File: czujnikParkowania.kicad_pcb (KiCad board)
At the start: 2 copper layers, 43 parts, among them J1 Screw_Terminal_01x03, Q1 BC817, Q2 IRF7404, Q3 BC817, Q4 BC817, Q5 BC817, U1 DC56-11SEKWA, U2 LM7805_TO220, U3 HC-SR04, U4 ATmega328-AU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

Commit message: missing connections on PCB
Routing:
- net Net-(R9-Pad1): track 9.51 -> 28.3 mm, vias 0 -> 2
- net Net-(R10-Pad1): track 11.4 -> 24.3 mm, vias 0 -> 1
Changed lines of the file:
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@@
     (thickness 1.6)
     (drawings 0)
-    (tracks 368)
+    (tracks 382)
     (zones 0)
     (modules 43)
@@
   (segment (start 49.53 42.164) (end 49.53 43.1315) (width 0.25) (layer F.Cu) (net 36))
   (segment (start 48.5648 41.1988) (end 49.53 42.164) (width 0.25) (layer F.Cu) (net 36))
+  (via (at 40.005 34.29) (size 0.8) (drill 0.4) (layers F.Cu B.Cu) (net 36))
+  (segment (start 42.926 38.989) (end 42.926 37.211) (width 0.25) (layer F.Cu) (net 36))
+  (segment (start 42.926 37.211) (end 40.005 34.29) (width 0.25) (layer F.Cu) (net 36))
+  (via (at 36.83 34.29) (size 0.8) (drill 0.4) (layers F.Cu B.Cu) (net 36))
+  (segment (start 40.005 34.29) (end 36.83 34.29) (width 0.25) (layer B.Cu) (net 36))
+  (segment (start 36.83 34.29) (end 33.02 34.29) (width 0.25) (layer F.Cu) (net 36))
+  (segment (start 30.226 37.084) (end 30.226 38.989) (width 0.25) (layer F.Cu) (net 36))
+  (segment (start 33.02 34.29) (end 30.226 37.084) (width 0.25) (layer F.Cu) (net 36))
   (segment (start 46.228 43.1315) (end 45.477498 43.1315) (width 0.25) (layer F.Cu) (net 37))
   (segment (start 37.846 38.989) (end 37.846 38.481) (width 0.25) (layer F.Cu) (net 37))
@@
   (segment (start 45.0065 41.91) (end 46.228 43.1315) (width 0.25) (layer F.Cu) (net 37))
   (segment (start 42.8244 41.91) (end 45.0065 41.91) (width 0.25) (layer F.Cu) (net 37))
+  (via (at 33.655 36.83) (size 0.8) (drill 0.4) (layers F.Cu B.Cu) (net 37))
+  (segment (start 27.686 38.989) (end 29.845 36.83) (width 0.25) (layer B.Cu) (net 37))
+  (segment (start 29.845 36.83) (end 33.655 36.83) (width 0.25) (layer B.Cu) (net 37))
+  (segment (start 37.846 37.211) (end 37.846 38.989) (width 0.25) (layer F.Cu) (net 37))
+  (segment (start 33.655 36.83) (end 37.465 36.83) (width 0.25) (layer F.Cu) (net 37))
+  (segment (start 37.465 36.83) (end 37.846 37.211) (width 0.25) (layer F.Cu) (net 37))
   (segment (start 35.306 40.7416) (end 35.306 38.989) (width 0.25) (layer F.Cu) (net 38))
   (segment (start 26.4574 41.3004) (end 34.7472 41.3004) (width 0.25) (layer F.Cu) (net 38))

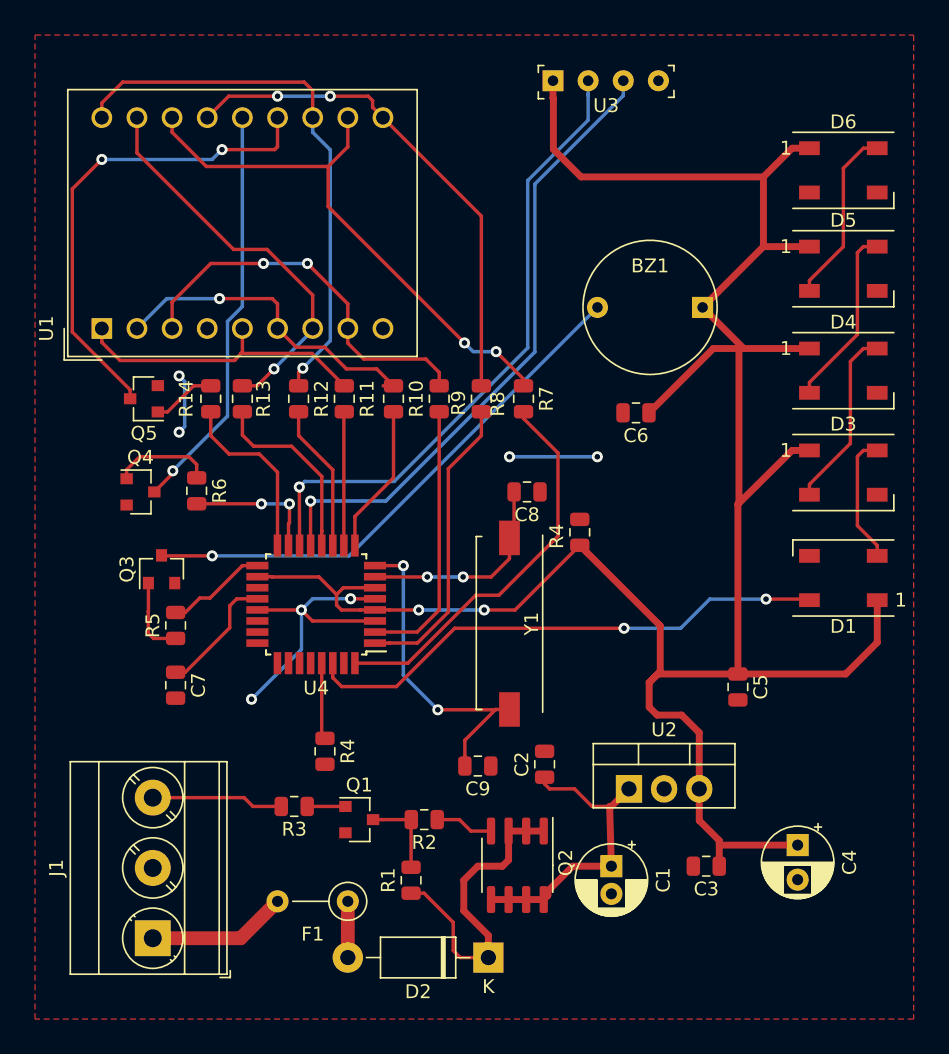
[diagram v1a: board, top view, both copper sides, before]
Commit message: added caps and button
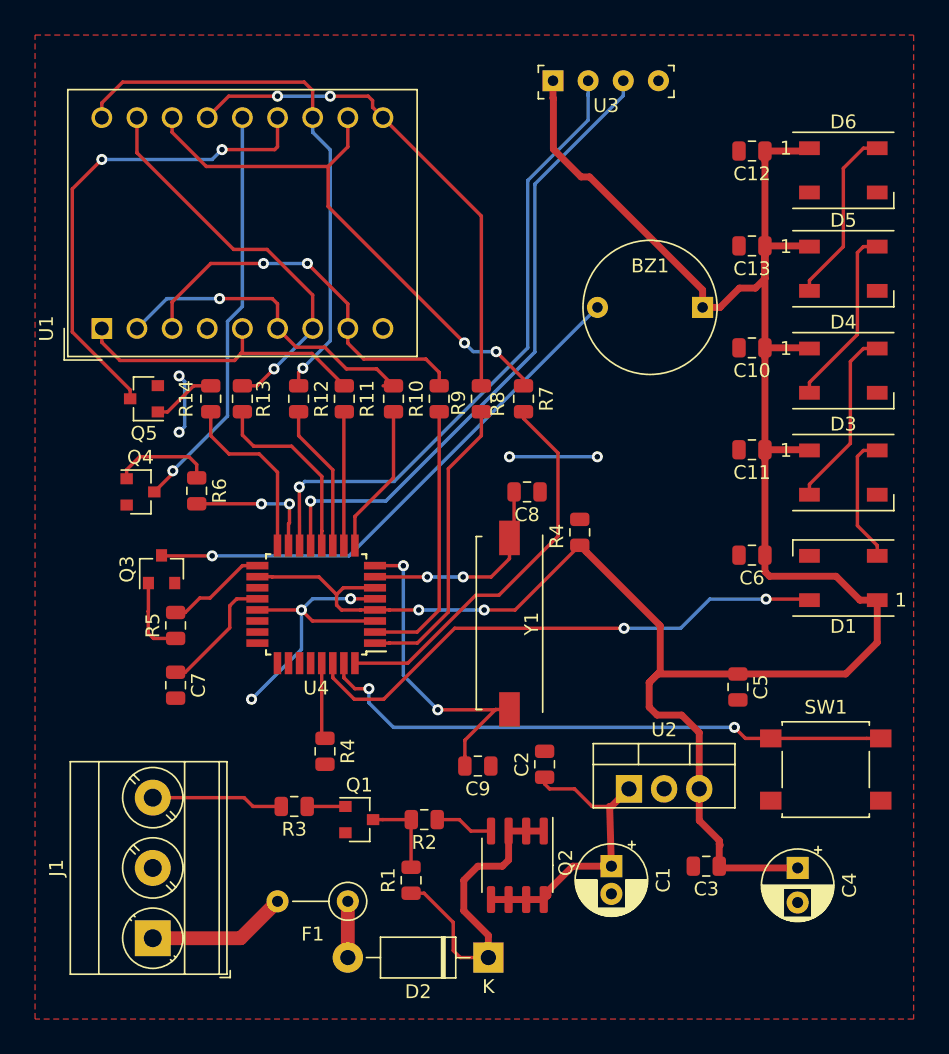
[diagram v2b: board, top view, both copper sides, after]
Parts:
- added C10: 100n, Capacitor_SMD:C_0805_2012Metric, F.Cu at (72.1, 40.4)
- added C11: 100n, Capacitor_SMD:C_0805_2012Metric, F.Cu at (72.1, 47.8)
- added C12: 100n, Capacitor_SMD:C_0805_2012Metric, F.Cu at (72.1, 26.2)
- added C13: 100n, Capacitor_SMD:C_0805_2012Metric, F.Cu at (72.1, 33.0)
- added SW1: SW_Push, Button_Switch_SMD:SW_SPST_B3S-1000, F.Cu at (77.5, 70.9)
- moved C6 13.3 mm to (72.1, 55.4)
- moved C4 1.65 mm to (75.4, 78.0)
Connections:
- U4 pad 31: /D1 -> /BTN
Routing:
- net /BTN: track 0.00 -> 42.3 mm, vias 0 -> 2
- net +5V: track 173.0 -> 166.7 mm
- net /RGB_DI: track 38.4 -> 39.2 mm

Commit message: added GND plane on back
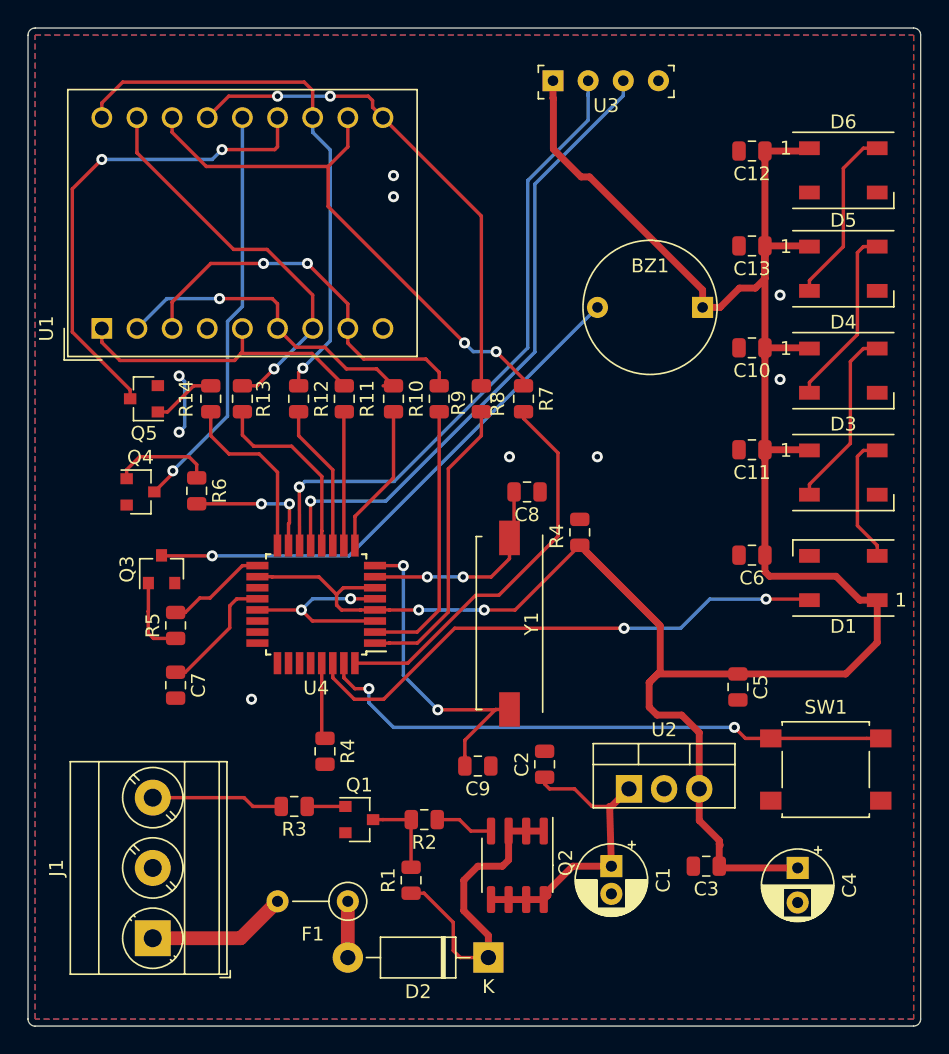
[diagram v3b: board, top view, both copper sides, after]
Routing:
- net GND: track 33.2 -> 18.9 mm, vias 7 -> 11
- net +5V: track 166.7 -> 174.1 mm
- added copper zone on B.Cu, net GND
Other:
- board outline added: 64.5 x 72.1 mm

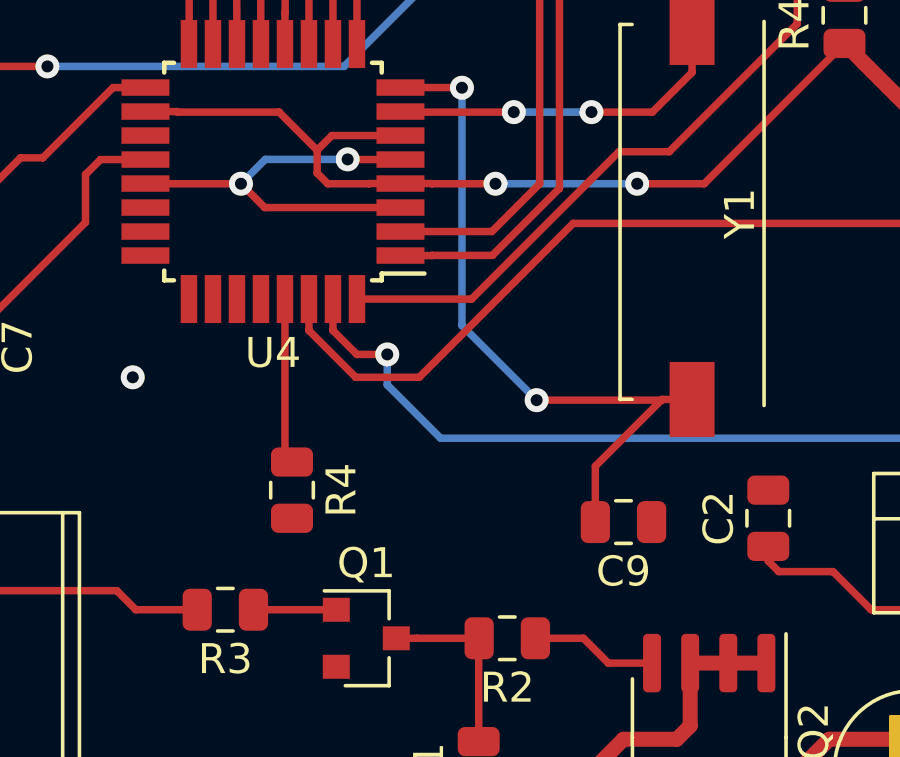
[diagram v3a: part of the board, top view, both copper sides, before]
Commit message: schematic reset pin bugfix
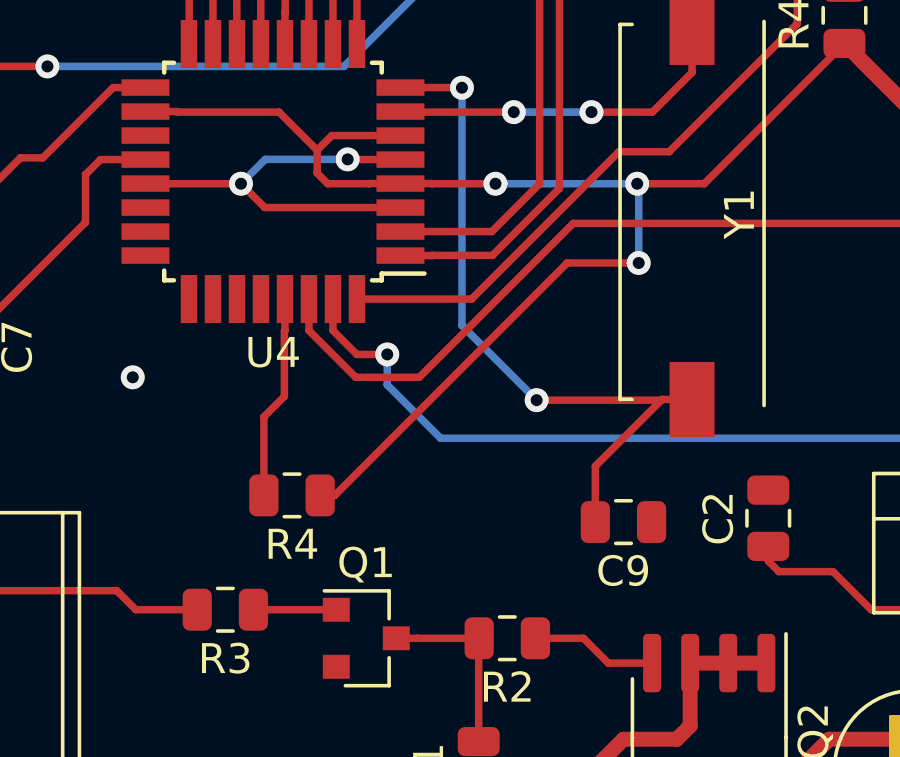
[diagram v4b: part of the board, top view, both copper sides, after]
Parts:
- moved R4 0.18 mm to (41.3, 69.7), turned to 180 degrees
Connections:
- R4 pad 1: Net-(R4-Pad1) -> +5V
- R4 pad 2: GND -> Net-(R4-Pad2)
- U4 pad 29: Net-(R4-Pad1) -> Net-(R4-Pad2)
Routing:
- net +5V: track 174.1 -> 190.6 mm, vias 2 -> 3
- net Net-(R4-Pad2): track 0.00 -> 6.84 mm
- net Net-(R4-Pad1): track 5.53 -> 0.00 mm
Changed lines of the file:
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@@
     (thickness 1.6)
     (drawings 8)
-    (tracks 408)
+    (tracks 417)
     (zones 0)
     (modules 48)
@@
   (net 46 "Net-(C8-Pad2)")
   (net 47 "Net-(C9-Pad2)")
-  (net 48 "Net-(R4-Pad1)")
-  (net 49 "Net-(U4-Pad19)")
-  (net 50 "Net-(U4-Pad22)")
-  (net 51 "Net-(U4-Pad23)")
-  (net 52 "Net-(U4-Pad24)")
-  (net 53 "Net-(U4-Pad25)")
-  (net 54 "Net-(U4-Pad26)")
-  (net 55 "Net-(U4-Pad27)")
-  (net 56 "Net-(U4-Pad28)")
-  (net 57 /BTN)
+  (net 48 "Net-(U4-Pad19)")
+  (net 49 "Net-(U4-Pad22)")
+  (net 50 "Net-(U4-Pad23)")
+  (net 51 "Net-(U4-Pad24)")
+  (net 52 "Net-(U4-Pad25)")
+  (net 53 "Net-(U4-Pad26)")
+  (net 54 "Net-(U4-Pad27)")
+  (net 55 "Net-(U4-Pad28)")
+  (net 56 /BTN)
+  (net 57 "Net-(R4-Pad2)")
   (net_class Default "To jest domyślna klasa połączeń."
     (clearance 0.2)
@@
     (add_net "Net-(R12-Pad1)")
     (add_net "Net-(R13-Pad1)")
-    (add_net "Net-(R4-Pad1)")
+    (add_net "Net-(R4-Pad2)")
     (add_net "Net-(R7-Pad1)")
     (add_net "Net-(R8-Pad1)")
@@
   )
   (module Resistor_SMD:R_0805_2012Metric (layer F.Cu)
-    (at 41.275 69.5475 270)
+    (at 41.275 69.723 180)
     (descr "Resistor SMD 0805 (2012 Metric), square (rectangular) end terminal, IPC_7351 nominal, (Body size source: https://docs.google.com/spreadsheets/d/1BsfQQcO9C6DZCsRaXUlFlo91Tg2WpOkGARC1WS5S8t0/edit?usp=sharing), generated with kicad-footprint-generator")
     (tags resistor)
     (attr smd)
-    (fp_text reference R4 (at 0 -1.65 90) (layer F.SilkS)
-      (effects (font (size 1 1) (thickness 0.15)))
-    )
-    (fp_text value 1k (at 0 1.65 90) (layer F.Fab)
+    (fp_text reference R4 (at 0 -1.65) (layer F.SilkS)
+      (effects (font (size 1 1) (thickness 0.15)))
+    )
+    (fp_text value 1k (at 0 1.65) (layer F.Fab)
       (effects (font (size 1 1) (thickness 0.15)))
     )
@@
     (fp_line (start 1.68 -0.95) (end 1.68 0.95) (layer F.CrtYd) (width 0.05))
     (fp_line (start 1.68 0.95) (end -1.68 0.95) (layer F.CrtYd) (width 0.05))
-    (fp_text user %R (at 0 0 90) (layer F.Fab)
+    (fp_text user %R (at 0 0) (layer F.Fab)
       (effects (font (size 0.5 0.5) (thickness 0.08)))
     )
-    (pad 1 smd roundrect (at -0.9375 0 270) (size 0.975 1.4) (layers F.Cu F.Paste F.Mask) (roundrect_rratio 0.25)
-      (net 48 "Net-(R4-Pad1)"))
-    (pad 2 smd roundrect (at 0.9375 0 270) (size 0.975 1.4) (layers F.Cu F.Paste F.Mask) (roundrect_rratio 0.25)
-      (net 4 GND))
+    (pad 1 smd roundrect (at -0.9375 0 180) (size 0.975 1.4) (layers F.Cu F.Paste F.Mask) (roundrect_rratio 0.25)
+      (net 2 +5V))
+    (pad 2 smd roundrect (at 0.9375 0 180) (size 0.975 1.4) (layers F.Cu F.Paste F.Mask) (roundrect_rratio 0.25)
+      (net 57 "Net-(R4-Pad2)"))
     (model ${KISYS3DMOD}/Resistor_SMD.3dshapes/R_0805_2012Metric.wrl
       (at (xyz 0 0 0))
@@
       (net 2 +5V))
     (pad 19 smd rect (at 4.25 1.2 180) (size 1.6 0.55) (layers F.Cu F.Paste F.Mask)
-      (net 49 "Net-(U4-Pad19)"))
+      (net 48 "Net-(U4-Pad19)"))
     (pad 20 smd rect (at 4.25 0.4 180) (size 1.6 0.55) (layers F.Cu F.Paste F.Mask)
       (net 45 "Net-(C7-Pad1)"))
@@
       (net 4 GND))
     (pad 22 smd rect (at 4.25 -1.2 180) (size 1.6 0.55) (layers F.Cu F.Paste F.Mask)
-      (net 50 "Net-(U4-Pad22)"))
+      (net 49 "Net-(U4-Pad22)"))
     (pad 23 smd rect (at 4.25 -2 180) (size 1.6 0.55) (layers F.Cu F.Paste F.Mask)
-      (net 51 "Net-(U4-Pad23)"))
+      (net 50 "Net-(U4-Pad23)"))
     (pad 24 smd rect (at 4.25 -2.8 180) (size 1.6 0.55) (layers F.Cu F.Paste F.Mask)
-      (net 52 "Net-(U4-Pad24)"))
+      (net 51 "Net-(U4-Pad24)"))
     (pad 25 smd rect (at 2.8 -4.25 270) (size 1.6 0.55) (layers F.Cu F.Paste F.Mask)
-      (net 53 "Net-(U4-Pad25)"))
+      (net 52 "Net-(U4-Pad25)"))
     (pad 26 smd rect (at 2 -4.25 270) (size 1.6 0.55) (layers F.Cu F.Paste F.Mask)
-      (net 54 "Net-(U4-Pad26)"))
+      (net 53 "Net-(U4-Pad26)"))
     (pad 27 smd rect (at 1.2 -4.25 270) (size 1.6 0.55) (layers F.Cu F.Paste F.Mask)
-      (net 55 "Net-(U4-Pad27)"))
+      (net 54 "Net-(U4-Pad27)"))
     (pad 28 smd rect (at 0.4 -4.25 270) (size 1.6 0.55) (layers F.Cu F.Paste F.Mask)
-      (net 56 "Net-(U4-Pad28)"))
+      (net 55 "Net-(U4-Pad28)"))
     (pad 29 smd rect (at -0.4 -4.25 270) (size 1.6 0.55) (layers F.Cu F.Paste F.Mask)
-      (net 48 "Net-(R4-Pad1)"))
+      (net 57 "Net-(R4-Pad2)"))
     (pad 30 smd rect (at -1.2 -4.25 270) (size 1.6 0.55) (layers F.Cu F.Paste F.Mask)
       (net 1 /RGB_DI))
     (pad 31 smd rect (at -2 -4.25 270) (size 1.6 0.55) (layers F.Cu F.Paste F.Mask)
-      (net 57 /BTN))
+      (net 56 /BTN))
     (pad 32 smd rect (at -2.8 -4.25 270) (size 1.6 0.55) (layers F.Cu F.Paste F.Mask)
       (net 5 /SEG_A))
@@
     (fp_line (start -3 3.3) (end -3 -3.3) (layer F.Fab) (width 0.1))
     (pad 1 smd rect (at -3.975 -2.25) (size 1.55 1.3) (layers F.Cu F.Paste F.Mask)
-      (net 57 /BTN))
+      (net 56 /BTN))
     (pad 1 smd rect (at 3.975 -2.25) (size 1.55 1.3) (layers F.Cu F.Paste F.Mask)
-      (net 57 /BTN))
+      (net 56 /BTN))
     (pad 2 smd rect (at -3.975 2.25) (size 1.55 1.3) (layers F.Cu F.Paste F.Mask)
       (net 4 GND))
@@
   (segment (start 65.44425 60.41275) (end 59.69 54.6585) (width 0.5) (layer F.Cu) (net 2) (status 20))
   (segment (start 65.44425 60.41275) (end 60.175527 55.144027) (width 0.5) (layer F.Cu) (net 2))
+  (segment (start 50.447 61.976) (end 52.832 61.976) (width 0.25) (layer F.Cu) (net 2))
+  (segment (start 42.2125 69.723) (end 42.7 69.723) (width 0.25) (layer F.Cu) (net 2))
+  (via (at 52.832 61.976) (size 0.8) (drill 0.4) (layers F.Cu B.Cu) (net 2))
+  (segment (start 42.7 69.723) (end 50.447 61.976) (width 0.25) (layer F.Cu) (net 2))
+  (segment (start 52.832 59.3852) (end 52.7812 59.3344) (width 0.25) (layer B.Cu) (net 2))
+  (segment (start 52.832 61.976) (end 52.832 59.3852) (width 0.25) (layer B.Cu) (net 2))
   (via (at 46.228 29.464) (size 0.8) (drill 0.4) (layers F.Cu B.Cu) (net 4))
   (via (at 46.228 27.94) (size 0.8) (drill 0.4) (layers F.Cu B.Cu) (net 4))
@@
   (segment (start 53.587 66.548) (end 53.61 66.525) (width 0.25) (layer F.Cu) (net 47))
   (segment (start 49.4284 66.548) (end 53.587 66.548) (width 0.25) (layer F.Cu) (net 47))
-  (segment (start 41.04 68.375) (end 41.275 68.61) (width 0.25) (layer F.Cu) (net 48) (status 30))
-  (segment (start 41.04 63.178) (end 41.04 68.375) (width 0.25) (layer F.Cu) (net 48) (status 30))
-  (segment (start 80.42 68.616) (end 73.495 68.616) (width 0.25) (layer F.Cu) (net 57) (status 20))
-  (via (at 44.45 65.024) (size 0.8) (drill 0.4) (layers F.Cu B.Cu) (net 57))
-  (segment (start 43.436 65.024) (end 44.45 65.024) (width 0.25) (layer F.Cu) (net 57))
-  (segment (start 42.64 63.178) (end 42.64 64.228) (width 0.25) (layer F.Cu) (net 57) (status 10))
-  (segment (start 42.64 64.228) (end 43.436 65.024) (width 0.25) (layer F.Cu) (net 57))
-  (segment (start 44.45 65.024) (end 44.45 66.04) (width 0.25) (layer B.Cu) (net 57))
-  (via (at 70.866 67.818) (size 0.8) (drill 0.4) (layers F.Cu B.Cu) (net 57))
-  (segment (start 44.45 66.04) (end 46.228 67.818) (width 0.25) (layer B.Cu) (net 57))
-  (segment (start 46.228 67.818) (end 70.866 67.818) (width 0.25) (layer B.Cu) (net 57))
-  (segment (start 71.664 68.616) (end 73.495 68.616) (width 0.25) (layer F.Cu) (net 57) (status 20))
-  (segment (start 70.866 67.818) (end 71.664 68.616) (width 0.25) (layer F.Cu) (net 57))
-  (segment (start 81.445 68.616) (end 80.42 68.616) (width 0.25) (layer F.Cu) (net 57) (status 10))
+  (segment (start 80.42 68.616) (end 73.495 68.616) (width 0.25) (layer F.Cu) (net 56) (status 20))
+  (via (at 44.45 65.024) (size 0.8) (drill 0.4) (layers F.Cu B.Cu) (net 56))
+  (segment (start 43.436 65.024) (end 44.45 65.024) (width 0.25) (layer F.Cu) (net 56))
+  (segment (start 42.64 63.178) (end 42.64 64.228) (width 0.25) (layer F.Cu) (net 56) (status 10))
+  (segment (start 42.64 64.228) (end 43.436 65.024) (width 0.25) (layer F.Cu) (net 56))
+  (segment (start 44.45 65.024) (end 44.45 66.04) (width 0.25) (layer B.Cu) (net 56))
+  (via (at 70.866 67.818) (size 0.8) (drill 0.4) (layers F.Cu B.Cu) (net 56))
+  (segment (start 44.45 66.04) (end 46.228 67.818) (width 0.25) (layer B.Cu) (net 56))
+  (segment (start 46.228 67.818) (end 70.866 67.818) (width 0.25) (layer B.Cu) (net 56))
+  (segment (start 71.664 68.616) (end 73.495 68.616) (width 0.25) (layer F.Cu) (net 56) (status 20))
+  (segment (start 70.866 67.818) (end 71.664 68.616) (width 0.25) (layer F.Cu) (net 56))
+  (segment (start 81.445 68.616) (end 80.42 68.616) (width 0.25) (layer F.Cu) (net 56) (status 10))
+  (segment (start 41.04 64.228) (end 41.021 64.247) (width 0.25) (layer F.Cu) (net 57))
+  (segment (start 41.04 63.178) (end 41.04 64.228) (width 0.25) (layer F.Cu) (net 57))
+  (segment (start 41.021 64.247) (end 41.021 66.421) (width 0.25) (layer F.Cu) (net 57))
+  (segment (start 40.3375 67.1045) (end 40.3375 69.723) (width 0.25) (layer F.Cu) (net 57))
+  (segment (start 41.021 66.421) (end 40.3375 67.1045) (width 0.25) (layer F.Cu) (net 57))
   (zone (net 4) (net_name GND) (layer F.Cu) (hatch edge 0.508)
     (connect_pads (clearance 0.508))
